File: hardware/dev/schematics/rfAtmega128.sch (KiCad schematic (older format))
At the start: 59 parts, among them J1 TEST_VDD33, J2 TEST_GND, J3 PWR_ON/OFF, J4 J2PIN, J5 J2PIN, U1 LED_RED, U10 LED_GREEN, U11 LED_GREEN, U12 LED_GREEN, U13 BAT54S, U14 BAT54S, U2 DIODE, U3 Q16.000, U4 BA033CC0WFP, U5 BUTTON, U6 ATMEGA128RFA1, U7 FT232RL, U8 2450FB15L0001, U9 LED_GREEN, X1 RP-SMA

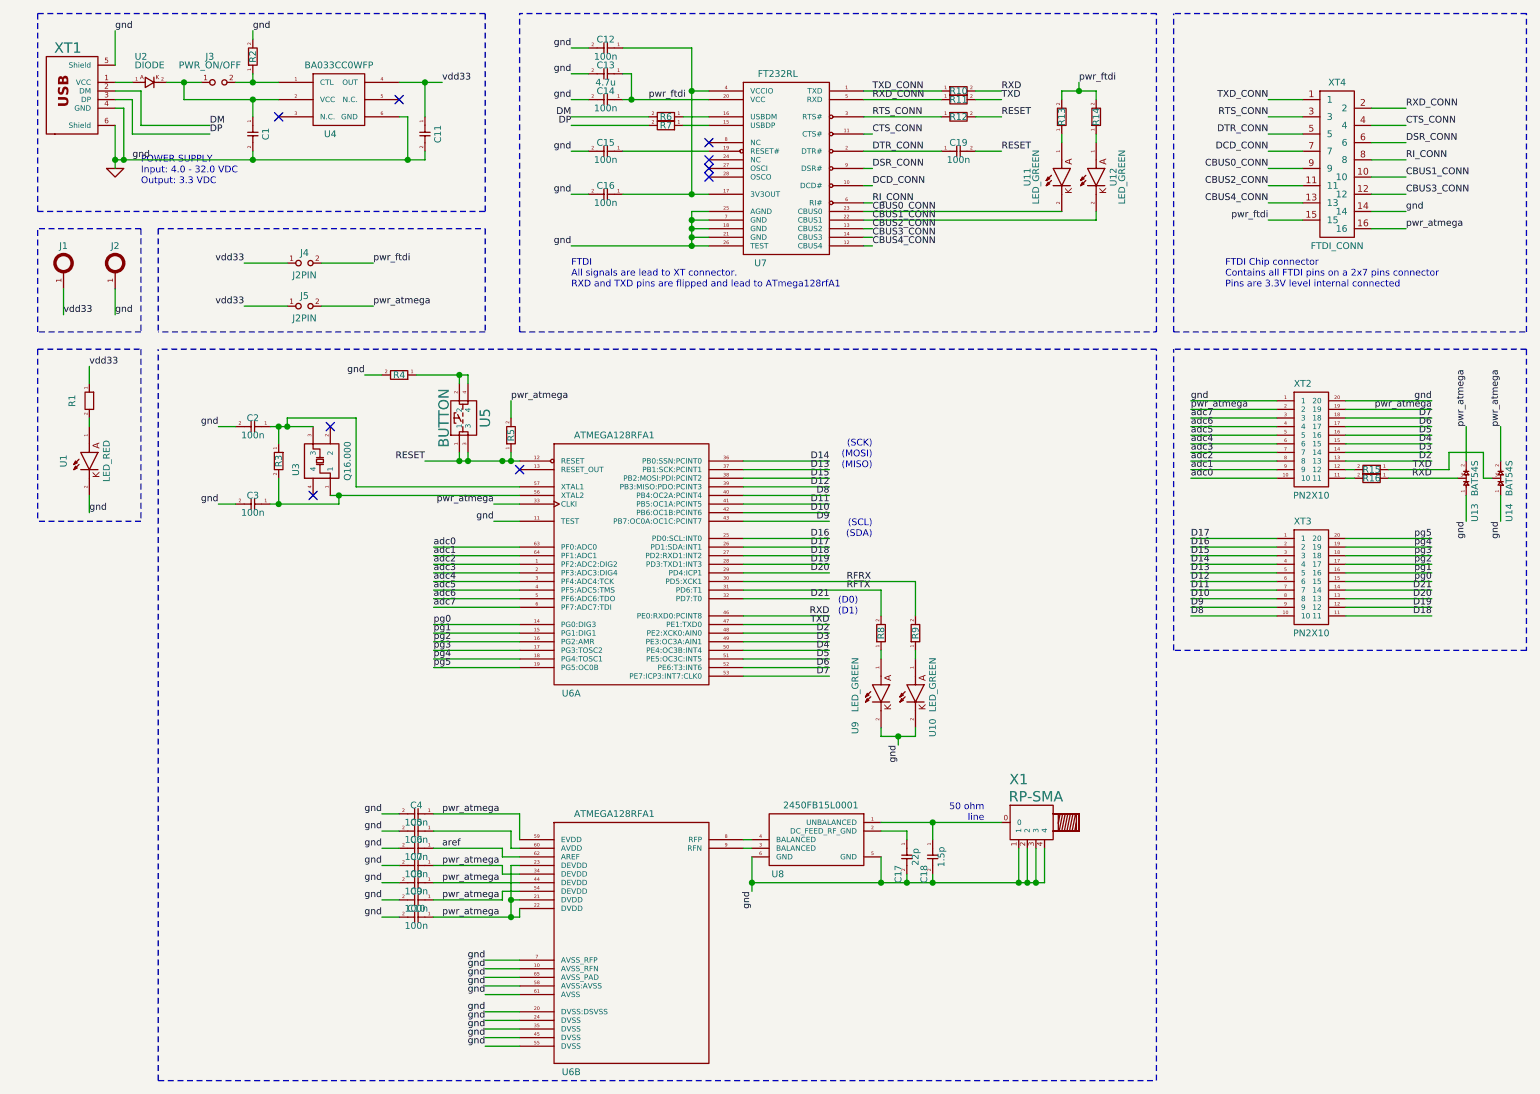
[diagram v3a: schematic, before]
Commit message: Board routing started and rf part done.
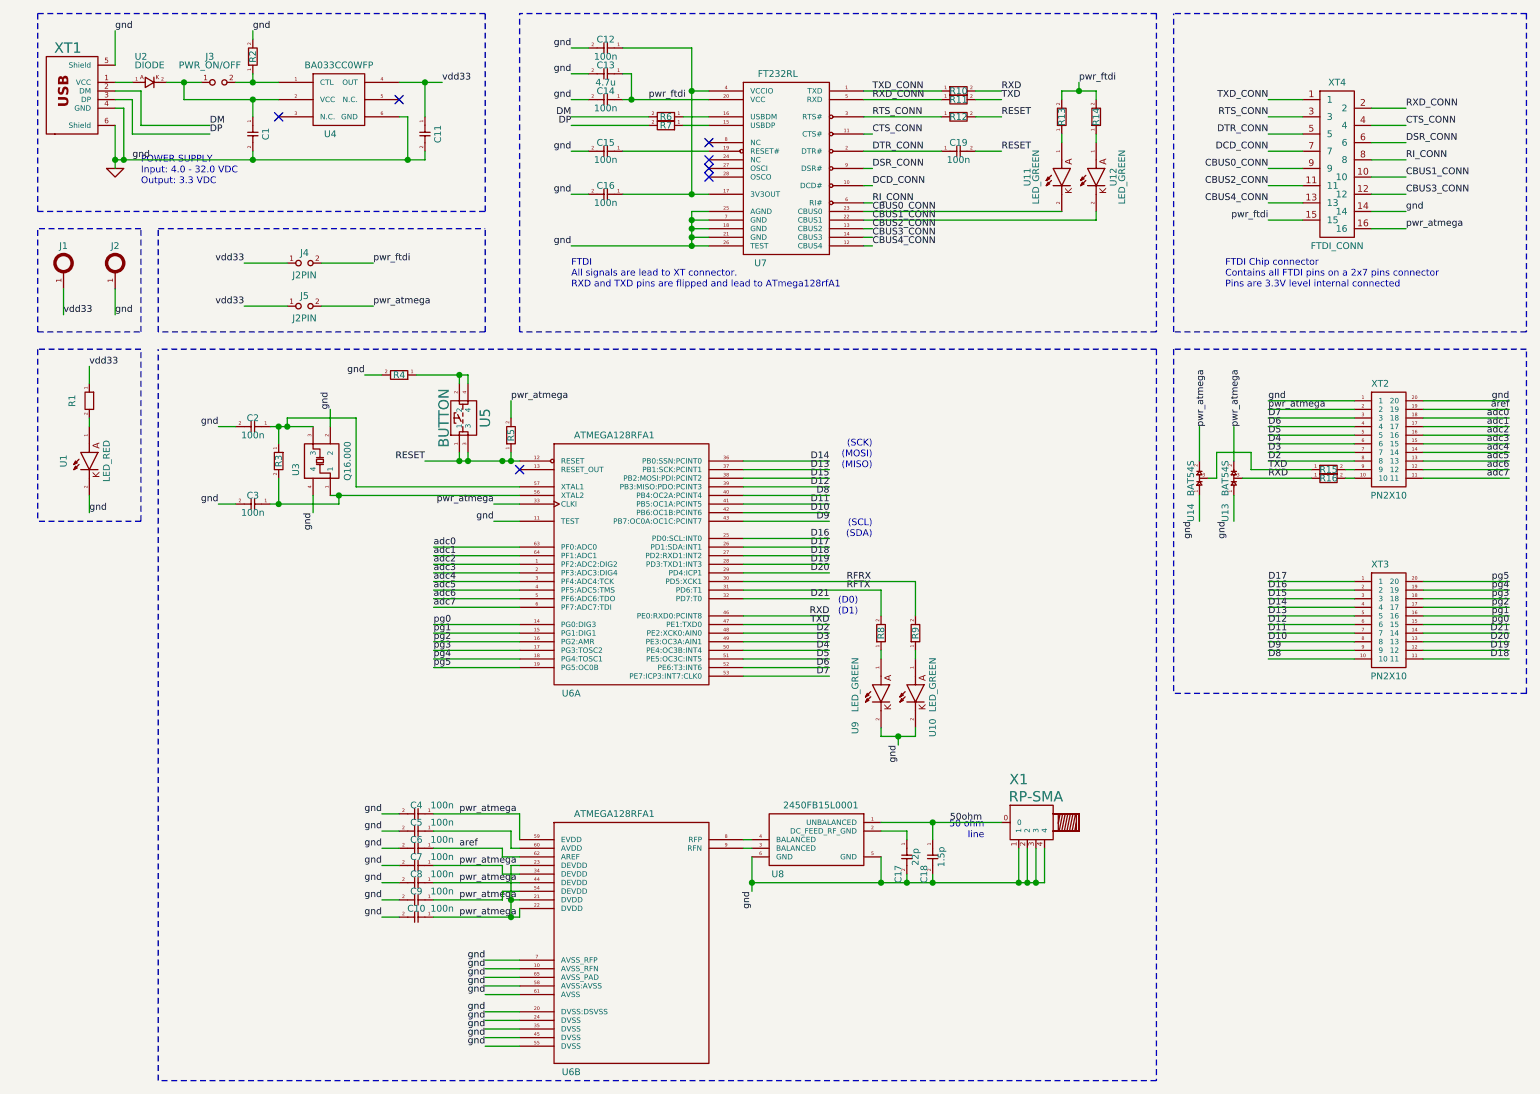
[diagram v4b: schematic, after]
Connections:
- net D2: now also XT2.8; no longer XT2.13
- net D3: now also XT2.7; no longer XT2.14
- net D4: now also XT2.6; no longer XT2.15
- net D5: now also XT2.5; no longer XT2.16
- net D6: now also XT2.4; no longer XT2.17
- net D7: now also XT2.3; no longer XT2.18
- net GND: now also U3.2, U3.4; no longer U13.1, U14.1
- net adc0: now also XT2.18; no longer XT2.10
- net adc1: now also XT2.17; no longer XT2.9
- net adc2: now also XT2.16; no longer XT2.8
- net adc3: now also XT2.15; no longer XT2.7
- net adc4: now also XT2.14; no longer XT2.6
- net adc5: now also XT2.13; no longer XT2.5
- net adc6: now also XT2.12; no longer XT2.4
- net adc7: now also XT2.11; no longer XT2.3
- net aref: now also XT2.19
- net pwr_atmega: no longer U13.2, U14.2, XT2.19
- net at R16.2: now also XT2.10; no longer XT2.11
- net at R15.2: now also XT2.9; no longer XT2.12
- net 50ohm: now reaches C18.1, U8.1 (UNBALANCED), X1.0
- no-connect marks 9 -> 7
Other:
- moved on the sheet: R15, R16, U13, U14, XT2, XT3

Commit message: Most of ATmega128rfA1 pins are connected now. Additional power connector should be added with 2.54 mm stepping near to digital pins.
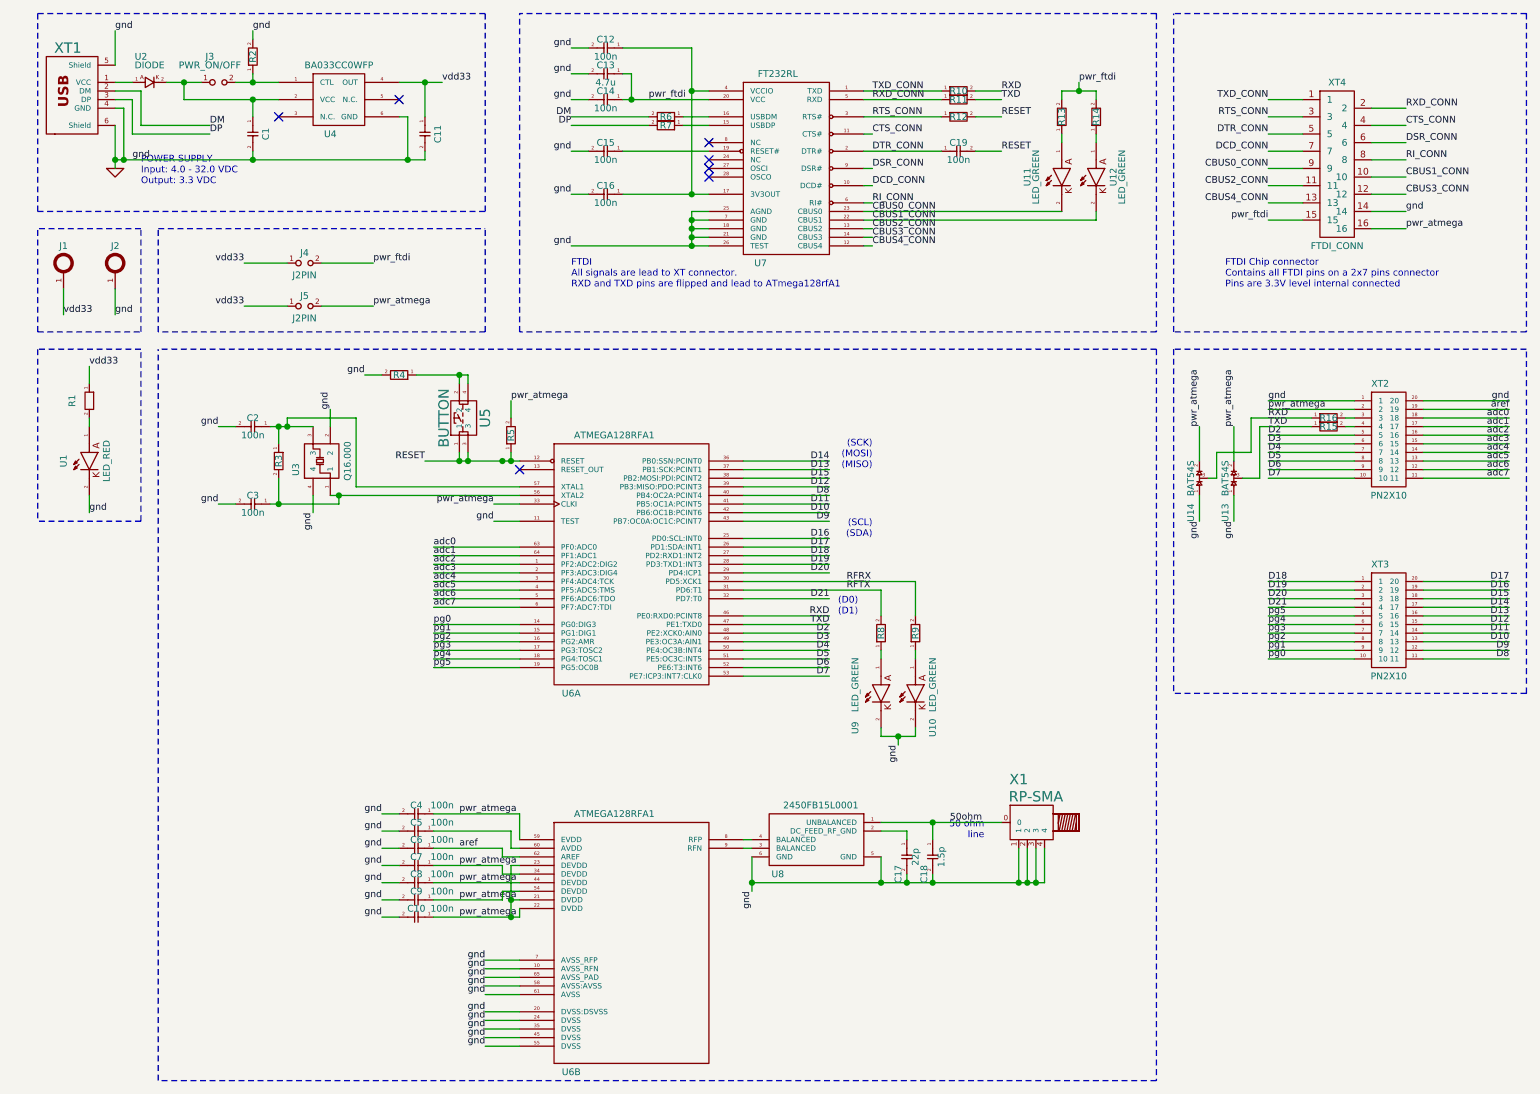
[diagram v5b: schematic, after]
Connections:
- net D10: now also XT3.13; no longer XT3.8
- net D11: now also XT3.14; no longer XT3.7
- net D12: now also XT3.15; no longer XT3.6
- net D13: now also XT3.16; no longer XT3.5
- net D14: now also XT3.17; no longer XT3.4
- net D15: now also XT3.18; no longer XT3.3
- net D16: now also XT3.19; no longer XT3.2
- net D17: now also XT3.20; no longer XT3.1
- net D18: now also XT3.1; no longer XT3.11
- net D19: now also XT3.2; no longer XT3.12
- net D2: now also XT2.5; no longer XT2.8
- net D20: now also XT3.3; no longer XT3.13
- net D21: now also XT3.4; no longer XT3.14
- net D3: now also XT2.6; no longer XT2.7
- net D4: now also XT2.7; no longer XT2.6
- net D5: now also XT2.8; no longer XT2.5
- net D6: now also XT2.9; no longer XT2.4
- net D7: now also XT2.10; no longer XT2.3
- net D8: now also XT3.11; no longer XT3.10
- net D9: now also XT3.12; no longer XT3.9
- net GND: now also U13.1, U14.1
- net RXD: now also U14.3; no longer U13.3
- net TXD: now also U13.3; no longer U14.3
- net pg0: now also XT3.10; no longer XT3.15
- net pg1: now also XT3.9; no longer XT3.16
- net pg2: now also XT3.8; no longer XT3.17
- net pg3: now also XT3.7; no longer XT3.18
- net pg4: now also XT3.6; no longer XT3.19
- net pg5: now also XT3.5; no longer XT3.20
- net pwr_atmega: now also U13.2, U14.2
- net at R16.2: now also XT2.3; no longer XT2.10
- net at R15.2: now also XT2.4; no longer XT2.9
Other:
- moved on the sheet: R15, R16
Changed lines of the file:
@@
-EESchema Schematic File Version 2  date Mon 28 May 2012 04:40:30 PM EEST
+EESchema Schematic File Version 2  date Wed 30 May 2012 02:09:17 PM EEST
 LIBS:power
 LIBS:conn
@@
 Sheet 1 1
 Title ""
-Date "28 may 2012"
+Date "30 may 2012"
 Rev ""
 Comp ""
@@
 Comment4 ""
 $EndDescr
+Wire Wire Line
+	8100 3100 7800 3100
+Wire Wire Line
+	7800 3100 7800 3400
+Wire Wire Line
+	7800 3400 7700 3400
+Wire Wire Line
+	8300 3050 8350 3050
 Wire Notes Line
 	7200 2650 7200 6900
@@
 	2400 3100 2400 3000
 Wire Wire Line
-	3150 2800 3150 2850
-Wire Wire Line
-	3200 2850 3200 2800
+	3150 2850 3150 2800
+Wire Wire Line
+	3200 2800 3200 2850
 Connection ~ 3200 3300
 Wire Wire Line
-	3200 3250 3200 3300
+	3200 3300 3200 3250
 Wire Wire Line
 	2700 2800 2600 2800
@@
 Connection ~ 5700 4900
 Wire Wire Line
-	5700 4900 5700 4950
+	5700 4950 5700 4900
 Wire Wire Line
 	5600 4400 5600 4450
 Wire Wire Line
-	5800 4850 5800 4900
+	5800 4900 5800 4850
 Wire Wire Line
 	5800 4400 5800 4450
@@
 	3500 5950 3500 5900
 Wire Wire Line
-	8100 3350 7750 3350
-Wire Wire Line
-	7750 3350 7750 3250
-Wire Wire Line
-	7750 3250 7550 3250
+	7550 3250 7750 3250
 Wire Wire Line
 	7550 3250 7550 3400
 Wire Wire Line
-	8300 3350 8350 3350
+	7850 3350 8350 3350
 Wire Wire Line
 	4800 3750 5300 3750
@@
 Connection ~ 2150 3100
 Wire Wire Line
-	2150 3050 2150 3100
+	2150 3100 2150 3050
 Wire Wire Line
 	2050 3100 2300 3100
@@
 Connection ~ 4500 1150
 Wire Wire Line
-	4500 1750 4500 900
+	4500 900  4500 1750
 Wire Wire Line
 	4500 900  4100 900
@@
 	1150 1250 1200 1250
 Wire Wire Line
-	1200 1250 1200 1550
+	1200 1550 1200 1250
 Connection ~ 1200 1550
 Wire Wire Line
@@
 	2800 1100 3050 1100
 Wire Wire Line
-	2950 1500 2950 1550
-Wire Wire Line
-	2950 1550 1150 1550
+	2950 1550 2950 1500
+Wire Wire Line
+	1150 1550 2950 1550
 Connection ~ 2850 1550
 Wire Wire Line
@@
 	3800 1300 4250 1300
 Wire Wire Line
-	4600 1850 4500 1850
-Wire Wire Line
-	4500 1850 4500 2050
+	4500 1850 4600 1850
+Wire Wire Line
+	4500 2050 4500 1850
 Wire Wire Line
 	4500 1900 4600 1900
@@
 	6650 1400 6650 1450
 Wire Wire Line
-	6650 1200 6650 1150
+	6650 1150 6650 1200
 Wire Wire Line
 	6650 1150 6850 1150
@@
 	4800 3800 5300 3800
 Wire Wire Line
-	7700 3400 8100 3400
-Wire Wire Line
 	8350 3300 7850 3300
 Wire Wire Line
 	8350 3150 7850 3150
 Wire Wire Line
-	8350 3050 7850 3050
-Wire Wire Line
 	8350 2950 7850 2950
 Wire Wire Line
 	8350 3000 7850 3000
 Wire Wire Line
-	8350 3100 7850 3100
-Wire Wire Line
 	8350 3200 7850 3200
 Wire Wire Line
 	8350 3250 7850 3250
 Wire Wire Line
-	8300 3400 8350 3400
+	7850 3400 8350 3400
 Wire Wire Line
 	7550 3400 7500 3400
@@
 	4800 3600 5300 3600
 Wire Wire Line
-	5600 4850 5600 4900
-Wire Wire Line
-	5600 4900 5800 4900
+	5600 4900 5600 4850
+Wire Wire Line
+	5800 4900 5600 4900
 Wire Wire Line
 	4800 4000 5800 4000
@@
 Connection ~ 3150 3300
 Wire Wire Line
-	3200 2800 2900 2800
+	2900 2800 3200 2800
 Connection ~ 3150 2800
 Wire Wire Line
@@
 Wire Notes Line
 	7300 2650 7300 4650
+Wire Wire Line
+	8300 3100 8350 3100
+Wire Wire Line
+	7750 3250 7750 3050
+Wire Wire Line
+	7750 3050 8100 3050
 Text Label 2300 3600 3    39   ~ 0
 gnd
@@
 	-1   0    0    -1
 $EndComp
-Text Label 9250 4300 2    39   ~ 0
+Text Label 7850 4150 0    39   ~ 0
 D21
-Text Label 9250 4350 2    39   ~ 0
+Text Label 7850 4100 0    39   ~ 0
 D20
-Text Label 9250 4400 2    39   ~ 0
+Text Label 7850 4050 0    39   ~ 0
 D19
-Text Label 9250 4450 2    39   ~ 0
+Text Label 7850 4000 0    39   ~ 0
 D18
-Text Label 7850 4000 0    39   ~ 0
+Text Label 9250 4000 2    39   ~ 0
 D17
-Text Label 7850 4050 0    39   ~ 0
+Text Label 9250 4050 2    39   ~ 0
 D16
 Text Notes 5550 3350 2    39   ~ 0
@@
 Text Notes 5550 3750 2    39   ~ 0
 (SCL)\n(SDA)
-Text Label 9250 4000 2    39   ~ 0
+Text Label 7850 4200 0    39   ~ 0
 pg5
-Text Label 9250 4050 2    39   ~ 0
+Text Label 7850 4250 0    39   ~ 0
 pg4
+Text Label 7850 4300 0    39   ~ 0
+pg3
+Text Label 7850 4350 0    39   ~ 0
+pg2
+Text Label 7850 4400 0    39   ~ 0
+pg1
+Text Label 7850 4450 0    39   ~ 0
+pg0
 Text Label 9250 4100 2    39   ~ 0
-pg3
+D15
 Text Label 9250 4150 2    39   ~ 0
-pg2
+D14
 Text Label 9250 4200 2    39   ~ 0
-pg1
+D13
 Text Label 9250 4250 2    39   ~ 0
-pg0
-Text Label 7850 4100 0    39   ~ 0
-D15
-Text Label 7850 4150 0    39   ~ 0
-D14
-Text Label 7850 4200 0    39   ~ 0
-D13
-Text Label 7850 4250 0    39   ~ 0
 D12
-Text Label 7850 4300 0    39   ~ 0
+Text Label 9250 4300 2    39   ~ 0
 D11
-Text Label 7850 4350 0    39   ~ 0
+Text Label 9250 4350 2    39   ~ 0
 D10
-Text Label 7850 4400 0    39   ~ 0
+Text Label 9250 4400 2    39   ~ 0
 D9
-Text Label 7850 4450 0    39   ~ 0
+Text Label 9250 4450 2    39   ~ 0
 D8
 Text Label 5400 4050 0    39   ~ 0
@@
 	1    0    0    1
 $EndComp
-Text Label 7412 3650 3    39   ~ 0
-gnd
-Text Label 7488 3100 1    39   ~ 0
+Text Label 7450 3650 3    39   ~ 0
+gnd
+Text Label 7450 3100 1    39   ~ 0
 pwr_atmega
 $Comp
 L RES_0603 R15
 U 1 1 4FBB5097
-P 8200 3350
-F 0 "R15" H 8200 3350 39  0000 C CNN
-F 1 "RES_0603" H 8200 3450 39  0001 C CNN
-F 2 "r_0603" H 8200 3350 60  0001 C CNN
-	1    8200 3350
+P 8200 3100
+F 0 "R15" H 8200 3100 39  0000 C CNN
+F 1 "RES_0603" H 8200 3200 39  0001 C CNN
+F 2 "r_0603" H 8200 3100 60  0001 C CNN
+	1    8200 3100
 	1    0    0    -1
 $EndComp
@@
 Text Label 7850 3000 0    39   ~ 0
 pwr_atmega
+Text Label 7850 3050 0    39   ~ 0
+RXD
+Text Label 7850 3100 0    39   ~ 0
+TXD
+Text Label 7850 3150 0    39   ~ 0
+D2
+Text Label 7850 3200 0    39   ~ 0
+D3
+Text Label 7850 3250 0    39   ~ 0
+D4
+Text Label 7850 3300 0    39   ~ 0
+D5
+Text Label 7850 3350 0    39   ~ 0
+D6
 Text Label 7850 3400 0    39   ~ 0
-RXD
-Text Label 7850 3350 0    39   ~ 0
-TXD
-Text Label 7850 3300 0    39   ~ 0
-D2
-Text Label 7850 3250 0    39   ~ 0
-D3
-Text Label 7850 3200 0    39   ~ 0
-D4
-Text Label 7850 3150 0    39   ~ 0
-D5
-Text Label 7850 3100 0    39   ~ 0
-D6
-Text Label 7850 3050 0    39   ~ 0
 D7
 $Comp
 L RES_0603 R16
 U 1 1 4FBB5096
-P 8200 3400
-F 0 "R16" H 8200 3400 39  0000 C CNN
-F 1 "RES_0603" H 8200 3500 39  0001 C CNN
-F 2 "r_0603" H 8200 3400 60  0001 C CNN
-	1    8200 3400
+P 8200 3050
+F 0 "R16" H 8200 3050 39  0000 C CNN
+F 1 "RES_0603" H 8200 3150 39  0001 C CNN
+F 2 "r_0603" H 8200 3050 60  0001 C CNN
+	1    8200 3050
 	1    0    0    -1
 $EndComp
@@
 	1    0    0    -1
 $EndComp
-Text Label 7688 3100 1    39   ~ 0
+Text Label 7650 3100 1    39   ~ 0
 pwr_atmega
 Text Label 5300 4550 2    39   ~ 0
@@
 	1    0    0    -1
 $EndComp
-Text Label 7612 3650 3    39   ~ 0
+Text Label 7650 3650 3    39   ~ 0
 gnd
 Text Label 3350 3650 2    39   ~ 0
